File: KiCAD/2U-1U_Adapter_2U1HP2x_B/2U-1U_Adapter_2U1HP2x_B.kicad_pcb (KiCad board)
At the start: 2 copper layers, 22.6 x 66.2 mm, 53 parts

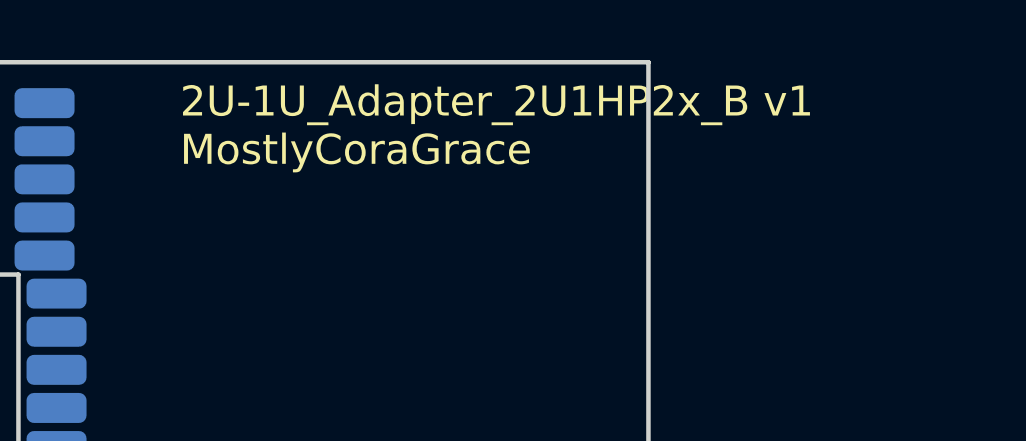
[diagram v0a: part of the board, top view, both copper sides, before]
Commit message: removed all front silkscreen, and flipped most modules, to make the boards 'cleaner'.
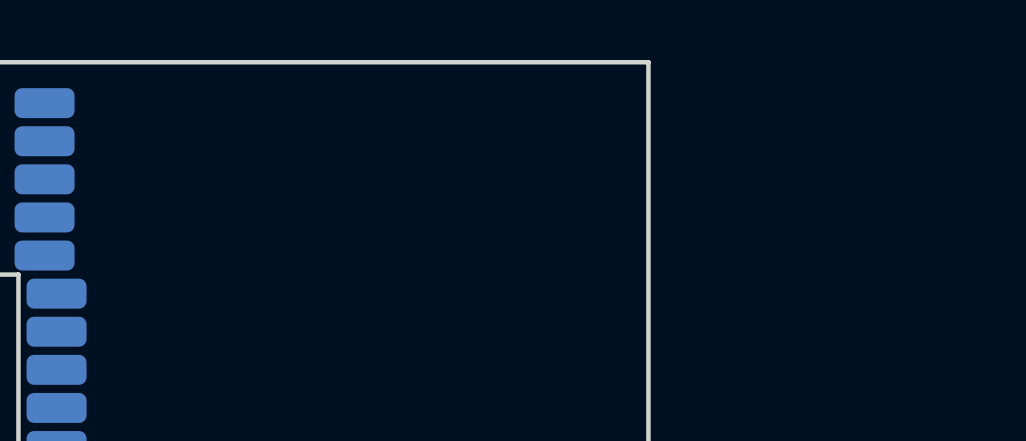
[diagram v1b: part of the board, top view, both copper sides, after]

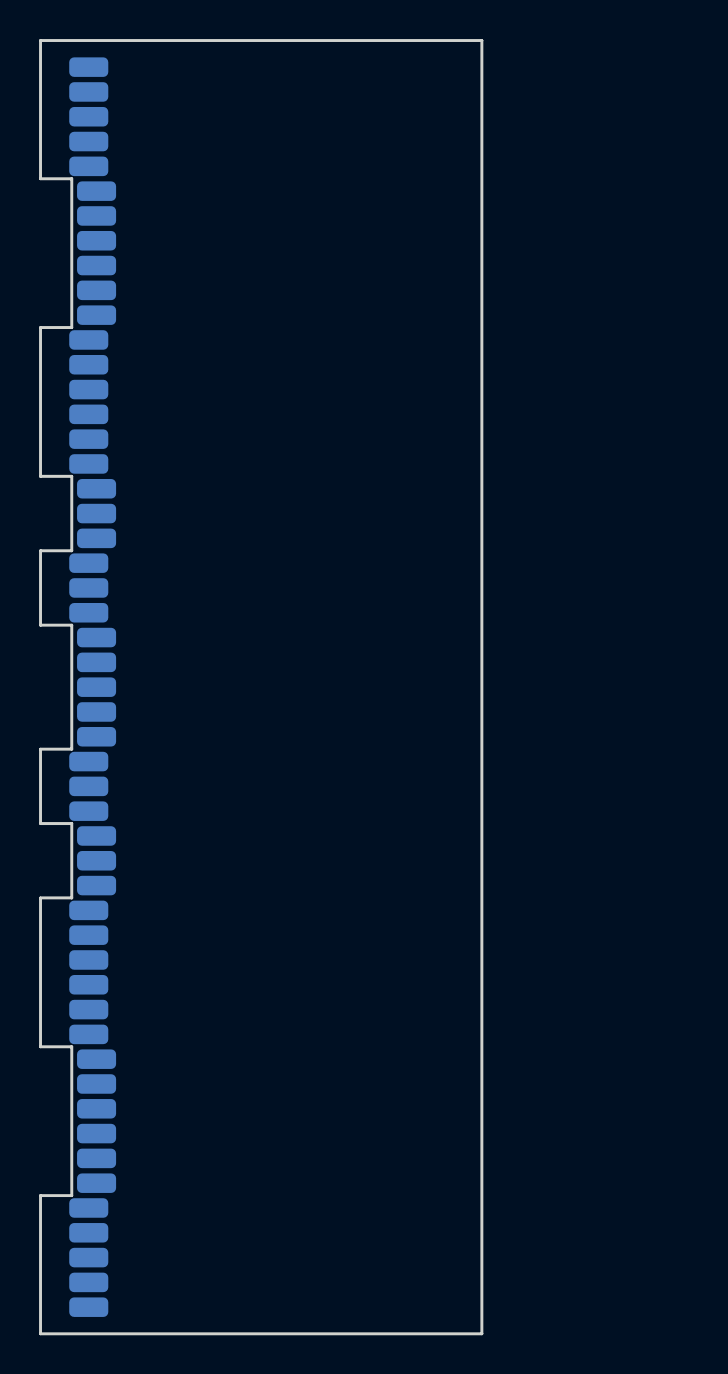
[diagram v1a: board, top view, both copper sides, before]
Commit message: added copper fills to every module, to maybe possibly increase structural rigidity.
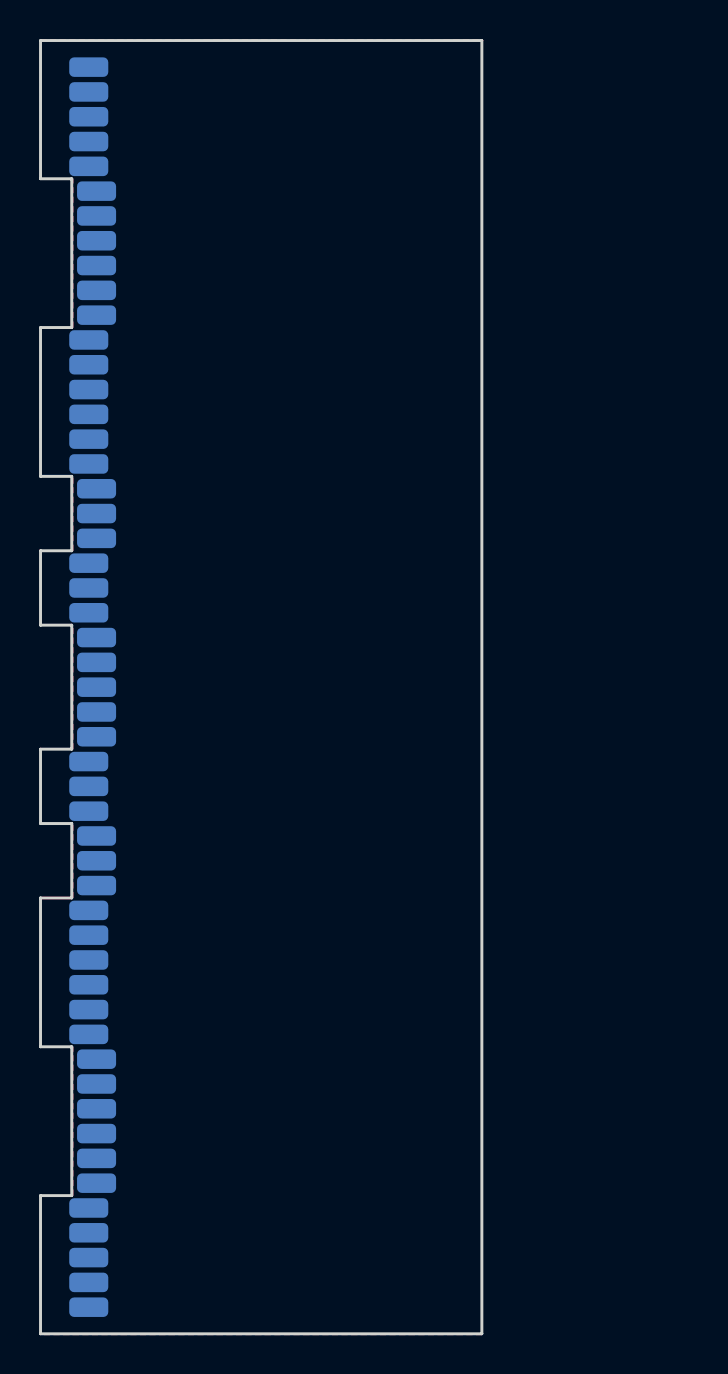
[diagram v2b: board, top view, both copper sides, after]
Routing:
- added copper zone on B.Cu, net (none)
- added copper zone on F.Cu, net (none)
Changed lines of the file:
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@@
+		)
+	)
+	(zone
+		(net 0)
+		(net_name "")
+		(layers "F&B.Cu")
+		(hatch edge 0.5)
+		(connect_pads
+			(clearance 0.5)
+		)
+		(min_thickness 0.25)
+		(filled_areas_thickness no)
+		(fill yes
+			(thermal_gap 0.5)
+			(thermal_bridge_width 0.5)
+			(island_removal_mode 1)
+			(island_area_min 10)
+		)
+		(polygon
+			(pts
+				(xy 0 11.303) (xy 22.606 11.303) (xy 22.606 77.597) (xy 0 77.597) (xy 0 70.485) (xy 1.651 70.485)
+				(xy 1.651 62.865) (xy 0 62.865) (xy 0 55.245) (xy 1.651 55.245) (xy 1.651 51.435) (xy 0 51.435)
+				(xy 0 47.625) (xy 1.651 47.625) (xy 1.651 41.275) (xy 0 41.275) (xy 0 37.465) (xy 1.651 37.465)
+				(xy 1.651 33.655) (xy 0 33.655) (xy 0 26.035) (xy 1.651 26.035) (xy 1.651 18.415) (xy 0 18.415)
+			)
 		)
 	)

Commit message: added PCBWay print identification silkscreen text to each component
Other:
- board text added: "WayWayWay"
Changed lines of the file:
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@@
+		)
+	)
+	(gr_text "WayWayWay"
+		(at 20.5 12 90)
+		(layer "B.SilkS")
+		(effects
+			(font
+				(size 1 1)
+				(thickness 0.15)
+			)
+			(justify left top mirror)
 		)
 	)
